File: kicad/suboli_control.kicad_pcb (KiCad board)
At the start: 2 copper layers, 125 x 95 mm, 45 parts, among them J1 DC barrel jack panel header 5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, J2 3.5 mm TRS input panel header, J4 3.5 mm TRS headphone panel he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, J5 MA12070 module power, J6 MA12070 module audio in, SW1 DPST power switch panel header, U1 TLE2426ILP

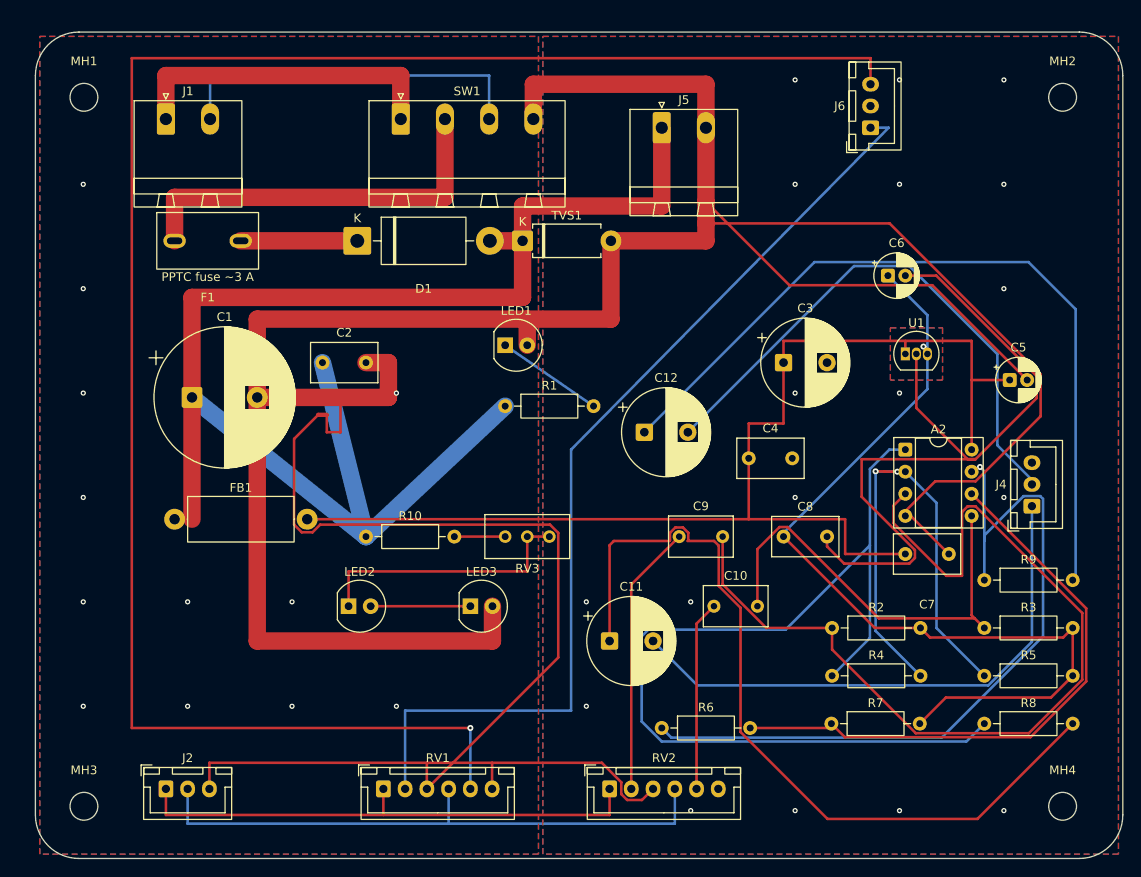
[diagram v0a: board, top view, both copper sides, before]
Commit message: R20: 8mm corner radius + re-export Gerbers + restore BOM
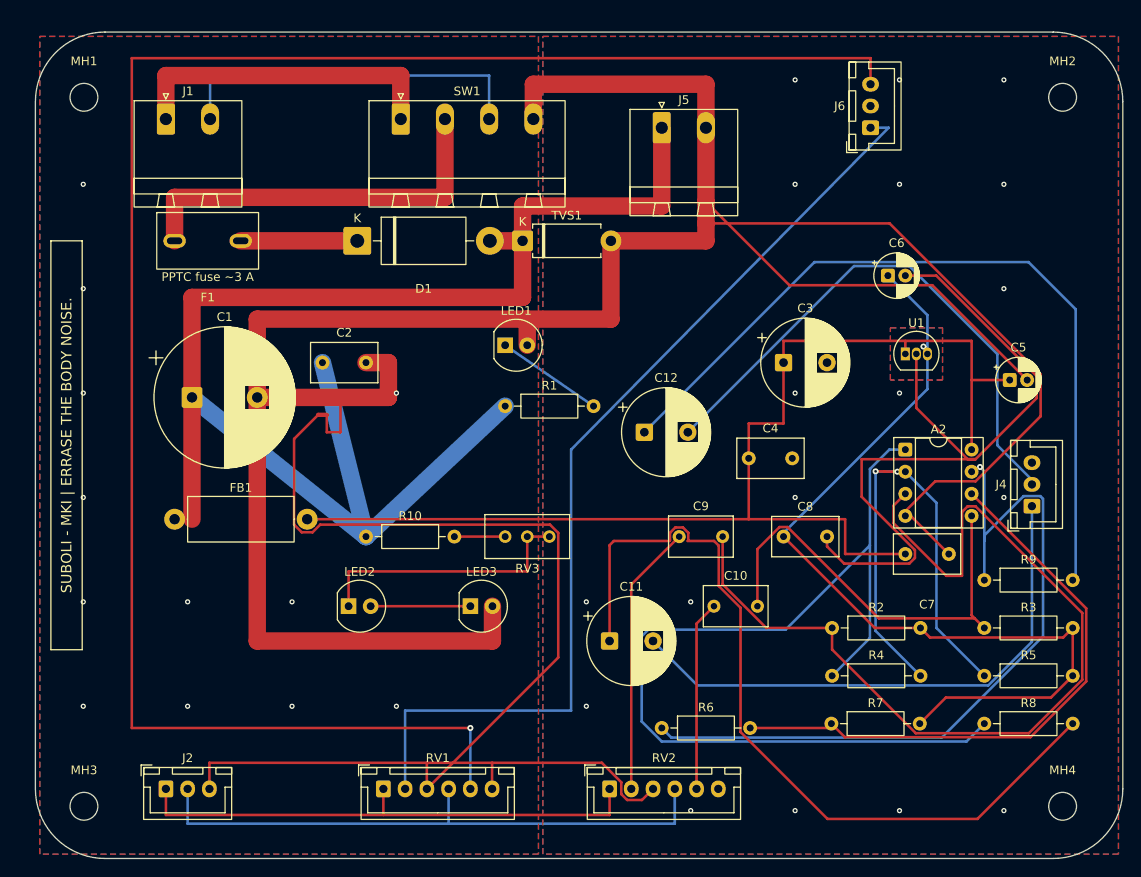
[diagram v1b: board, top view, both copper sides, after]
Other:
- outline, holes or cut-outs redrawn
- board text added: "SUBOLI - MKI | ERRASE THE BODY NOISE."
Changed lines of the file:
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@@
 		)
 	)
+	(gr_line
+		(start 13.7 36)
+		(end 17.3 36)
+		(stroke
+			(width 0.15)
+			(type default)
+		)
+		(layer "F.SilkS")
+	)
+	(gr_line
+		(start 13.7 83)
+		(end 13.7 36)
+		(stroke
+			(width 0.15)
+			(type default)
+		)
+		(layer "F.SilkS")
+	)
+	(gr_line
+		(start 17.3 36)
+		(end 17.3 83)
+		(stroke
+			(width 0.15)
+			(type default)
+		)
+		(layer "F.SilkS")
+	)
+	(gr_line
+		(start 17.3 83)
+		(end 13.7 83)
+		(stroke
+			(width 0.15)
+			(type default)
+		)
+		(layer "F.SilkS")
+	)
 	(gr_arc
-		(start 11.92 17)
-		(mid 13.384466 13.464466)
-		(end 16.92 12)
+		(start 11.92 20)
+		(mid 14.263146 14.343146)
+		(end 19.92 12)
 		(stroke
 			(width 0.15)
@@
 	)
 	(gr_line
-		(start 11.92 102)
-		(end 11.92 17)
+		(start 11.92 99)
+		(end 11.92 20)
 		(stroke
 			(width 0.15)
@@
 	)
 	(gr_line
-		(start 16.92 12)
-		(end 131.92 12)
+		(start 19.92 12)
+		(end 128.92 12)
 		(stroke
 			(width 0.15)
@@
 	)
 	(gr_arc
-		(start 16.92 107)
-		(mid 13.384466 105.535534)
-		(end 11.92 102)
+		(start 19.92 107)
+		(mid 14.263146 104.656854)
+		(end 11.92 99)
 		(stroke
 			(width 0.15)
@@
 	)
 	(gr_arc
-		(start 131.92 12)
-		(mid 135.455534 13.464466)
-		(end 136.92 17)
+		(start 128.92 12)
+		(mid 134.576854 14.343146)
+		(end 136.92 20)
 		(stroke
 			(width 0.15)
@@
 	)
 	(gr_line
-		(start 131.92 107)
-		(end 16.92 107)
+		(start 128.92 107)
+		(end 19.92 107)
 		(stroke
 			(width 0.15)
@@
 	)
 	(gr_line
-		(start 136.92 17)
-		(end 136.92 102)
+		(start 136.92 20)
+		(end 136.92 99)
 		(stroke
 			(width 0.15)
@@
 	)
 	(gr_arc
-		(start 136.92 102)
-		(mid 135.455534 105.535534)
-		(end 131.92 107)
+		(start 136.92 99)
+		(mid 134.576854 104.656854)
+		(end 128.92 107)
 		(stroke
 			(width 0.15)
@@
 		(layer "Edge.Cuts")
 	)
+	(gr_text "SUBOLI - MKI | ERRASE THE BODY NOISE."
+		(at 15.5 59.5 90)
+		(layer "F.SilkS")
+		(effects
+			(font
+				(size 1.2 1.2)
+				(thickness 0.15)
+			)
+		)
+	)
 	(segment

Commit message: R21: rotate J1/SW1/J5 180deg + relocate MH1 + clear connector traces for reroute
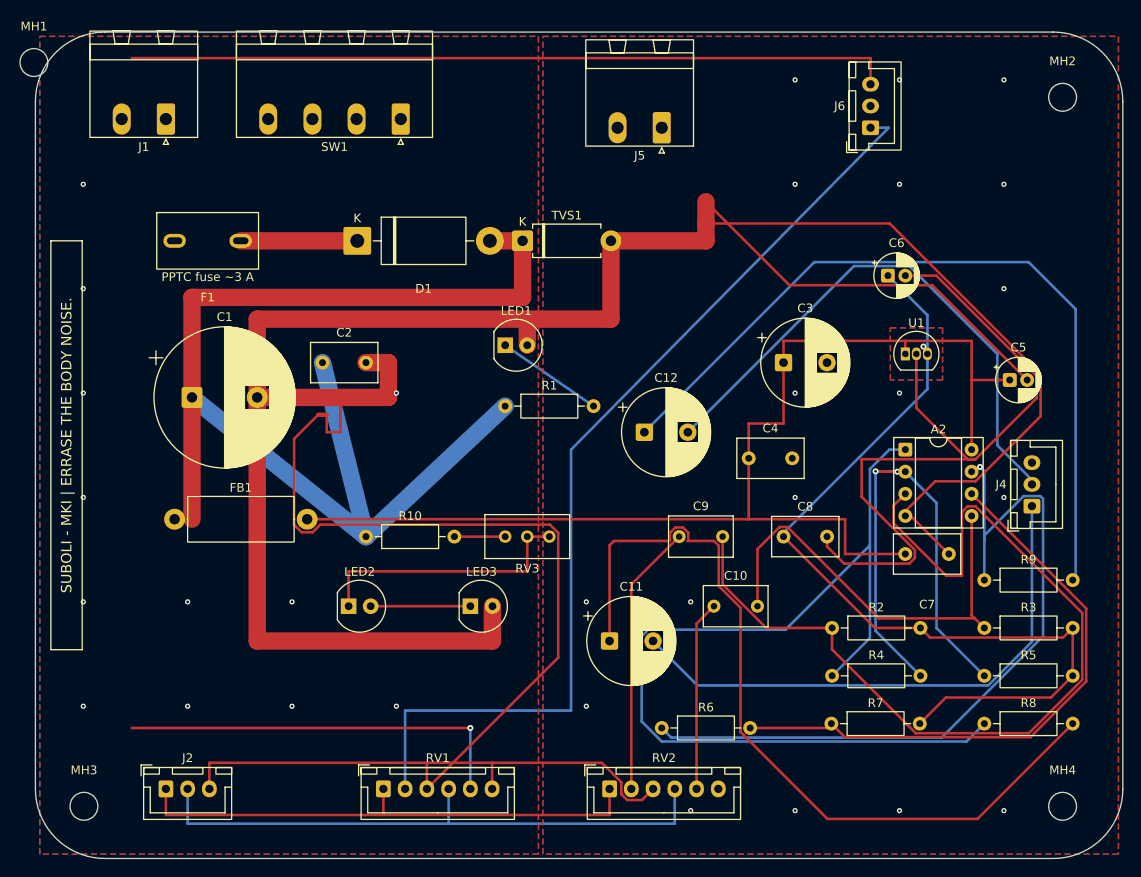
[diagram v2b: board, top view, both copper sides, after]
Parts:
- moved MH1 7.00 mm to (11.8, 15.5)
- turned J1 to 180 degrees
- turned J5 to 180 degrees
- turned SW1 to 180 degrees
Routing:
- net /TACT_INR: track 210.8 -> 133.8 mm
- net /+19V_SW: track 45.1 -> 0.00 mm
- net /GND_RAW: track 42.1 -> 0.00 mm
- net /GND_STAR: track 326.5 -> 289.2 mm
- net /+19V_RAW: track 37.0 -> 0.00 mm
- net /+19V: track 170.9 -> 141.9 mm

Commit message: R22: fix J1/SW1 placement clear of MH1 + reroute
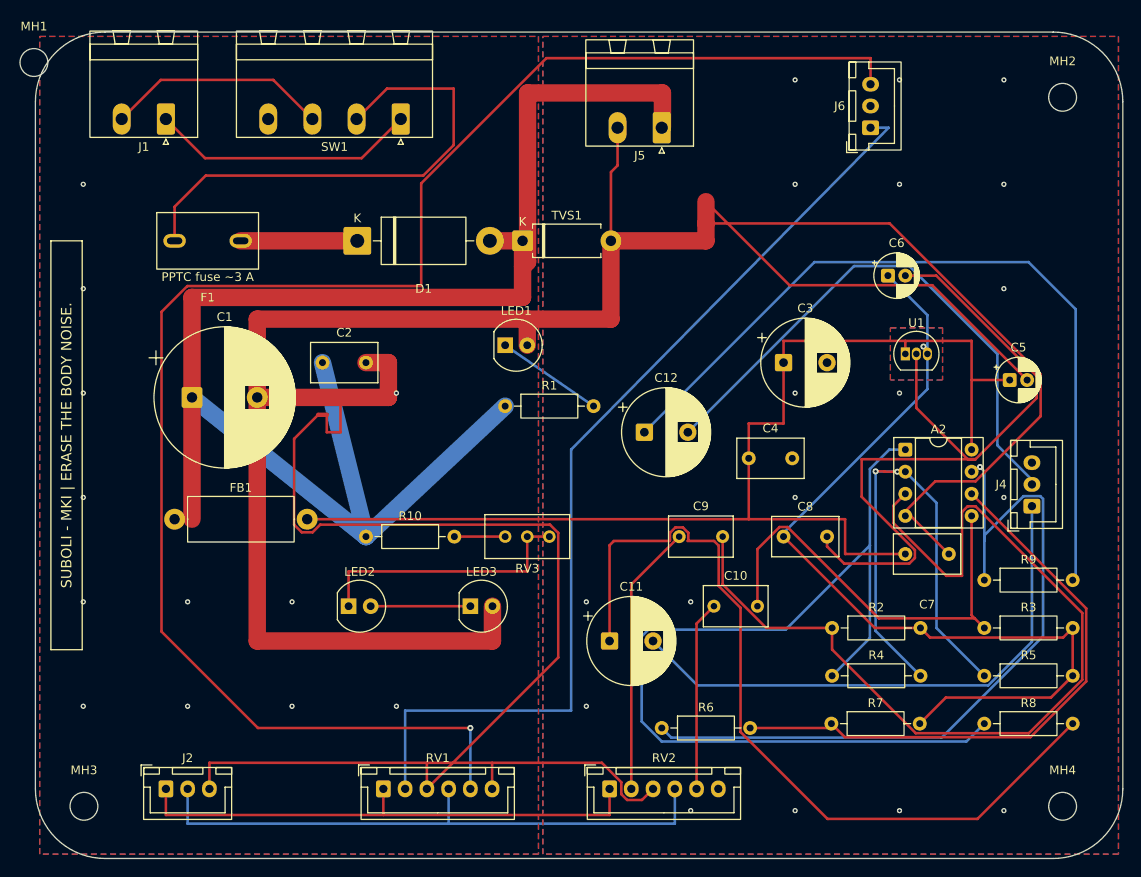
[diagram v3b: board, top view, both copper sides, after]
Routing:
- net /+19V_SW: track 0.00 -> 58.0 mm
- net /TACT_INR: track 133.8 -> 187.3 mm
- net /+19V: track 141.9 -> 181.7 mm
- net /+19V_RAW: track 0.00 -> 30.7 mm
- net /GND_RAW: track 0.00 -> 25.6 mm
- net /GND_STAR: track 289.2 -> 302.5 mm
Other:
- board text added: "SUBOLI - MKI | ERASE THE BODY NOISE."
- board text removed: "SUBOLI - MKI | ERRASE THE BODY NOISE."
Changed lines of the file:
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@@
 		(layer "Edge.Cuts")
 	)
-	(gr_text "SUBOLI - MKI | ERRASE THE BODY NOISE."
+	(gr_text "SUBOLI - MKI | ERASE THE BODY NOISE."
 		(at 15.5 59.5 90)
 		(layer "F.SilkS")
@@
 	)
 	(segment
+		(start 89 36)
+		(end 78.08 36)
+		(width 2)
+		(layer "F.Cu")
+		(net "/GND_STAR")
+	)
+	(segment
 		(start 37.42 54)
 		(end 52.5 54)
@@
 	)
 	(segment
+		(start 78.84 27.34)
+		(end 78.08 28.1)
+		(width 0.3)
+		(layer "F.Cu")
+		(net "/GND_STAR")
+	)
+	(segment
 		(start 52.5 54)
 		(end 52.5 50)
@@
 	)
 	(segment
+		(start 78.84 23)
+		(end 78.84 27.34)
+		(width 0.3)
+		(layer "F.Cu")
+		(net "/GND_STAR")
+	)
+	(segment
 		(start 47 54)
 		(end 47 58)
@@
 	)
 	(segment
+		(start 78.08 28.1)
+		(end 78.08 36)
+		(width 0.3)
+		(layer "F.Cu")
+		(net "/GND_STAR")
+	)
+	(segment
 		(start 47 58)
 		(end 45.42 58)
@@
 	)
 	(segment
-		(start 89 36)
-		(end 89 34)
-		(width 2)
-		(layer "F.Cu")
-		(net "/GND_STAR")
-	)
-	(segment
 		(start 111.62 67.62)
 		(end 111.5 67.5)
@@
 	)
 	(segment
-		(start 78.08 36)
+		(start 89 34)
 		(end 89 36)
 		(width 2)
@@
 	)
 	(segment
+		(start 49.42 26.5)
+		(end 31.42 26.5)
+		(width 0.3)
+		(layer "F.Cu")
+		(net "/+19V_RAW")
+	)
+	(segment
+		(start 31.42 26.5)
+		(end 26.92 22)
+		(width 0.3)
+		(layer "F.Cu")
+		(net "/+19V_RAW")
+	)
+	(segment
+		(start 53.92 22)
+		(end 49.42 26.5)
+		(width 0.3)
+		(layer "F.Cu")
+		(net "/+19V_RAW")
+	)
+	(segment
+		(start 56.5 28.5)
+		(end 31.5 28.5)
+		(width 0.3)
+		(layer "F.Cu")
+		(net "/+19V_SW")
+	)
+	(segment
+		(start 60 18.5)
+		(end 60 25)
+		(width 0.3)
+		(layer "F.Cu")
+		(net "/+19V_SW")
+	)
+	(segment
+		(start 52.34 18.5)
+		(end 60 18.5)
+		(width 0.3)
+		(layer "F.Cu")
+		(net "/+19V_SW")
+	)
+	(segment
+		(start 31.5 28.5)
+		(end 27.92 32.08)
+		(width 0.3)
+		(layer "F.Cu")
+		(net "/+19V_SW")
+	)
+	(segment
+		(start 60 25)
+		(end 56.5 28.5)
+		(width 0.3)
+		(layer "F.Cu")
+		(net "/+19V_SW")
+	)
+	(segment
+		(start 48.84 22)
+		(end 52.34 18.5)
+		(width 0.3)
+		(layer "F.Cu")
+		(net "/+19V_SW")
+	)
+	(segment
+		(start 27.92 32.08)
+		(end 27.92 36)
+		(width 0.3)
+		(layer "F.Cu")
+		(net "/+19V_SW")
+	)
+	(segment
+		(start 26.34 17.5)
+		(end 21.84 22)
+		(width 0.3)
+		(layer "F.Cu")
+		(net "/GND_RAW")
+	)
+	(segment
+		(start 39.26 17.5)
+		(end 26.34 17.5)
+		(width 0.3)
+		(layer "F.Cu")
+		(net "/GND_RAW")
+	)
+	(segment
+		(start 43.76 22)
+		(end 39.26 17.5)
+		(width 0.3)
+		(layer "F.Cu")
+		(net "/GND_RAW")
+	)
+	(segment
 		(start 95.932247 80.5)
 		(end 90.92 75.487753)
@@
 	)
 	(segment
+		(start 67.92 39)
+		(end 67.92 42.5)
+		(width 2)
+		(layer "F.Cu")
+		(net "/+19V")
+	)
+	(segment
 		(start 67.92 36)
-		(end 67.92 42.5)
+		(end 67.92 39)
 		(width 2)
 		(layer "F.Cu")
@@
 	)
 	(segment
+		(start 68.5 19)
+		(end 84 19)
+		(width 2)
+		(layer "F.Cu")
+		(net "/+19V")
+	)
+	(segment
 		(start 67.92 42.5)
 		(end 29.92 42.5)
@@
 	)
 	(segment
+		(start 84 22.92)
+		(end 83.92 23)
+		(width 2)
+		(layer "F.Cu")
+		(net "/+19V")
+	)
+	(segment
+		(start 84 19)
+		(end 84 22.92)
+		(width 2)
+		(layer "F.Cu")
+		(net "/+19V")
+	)
+	(segment
+		(start 67.92 39)
+		(end 68.5 38.42)
+		(width 2)
+		(layer "F.Cu")
+		(net "/+19V")
+	)
+	(segment
+		(start 68.5 38.42)
+		(end 68.5 19)
+		(width 2)
+		(layer "F.Cu")
+		(net "/+19V")
+	)
+	(segment
 		(start 49.92 70)
 		(end 65.92 55)
@@
 	)
 	(segment
+		(start 26.418 80.918)
+		(end 26.418 44.160694)
+		(width 0.3)
+		(layer "F.Cu")
+		(net "/TACT_INR")
+	)
+	(segment
+		(start 37.5 92)
+		(end 26.418 80.918)
+		(width 0.3)
+		(layer "F.Cu")
+		(net "/TACT_INR")
+	)
+	(segment
+		(start 29.380694 41.198)
+		(end 56.272165 41.198)
+		(width 0.3)
+		(layer "F.Cu")
+		(net "/TACT_INR")
+	)
+	(segment
+		(start 56.272165 41.198)
+		(end 56.272165 29.386529)
+		(width 0.3)
+		(layer "F.Cu")
+		(net "/TACT_INR")
+	)
+	(segment
+		(start 56.272165 29.386529)
+		(end 70.658694 15)
+		(width 0.3)
+		(layer "F.Cu")
+		(net "/TACT_INR")
+	)
+	(segment
+		(start 70.658694 15)
+		(end 107.92 15)
+		(width 0.3)
+		(layer "F.Cu")
+		(net "/TACT_INR")
+	)
+	(segment
+		(start 26.418 44.160694)
+		(end 29.380694 41.198)
+		(width 0.3)
+		(layer "F.Cu")
+		(net "/TACT_INR")
+	)
+	(segment
 		(start 61.92 92)
-		(end 23 92)
-		(width 0.3)
-		(layer "F.Cu")
-		(net "/TACT_INR")
-	)
-	(segment
-		(start 23 15)
-		(end 107.92 15)
-		(width 0.3)
-		(layer "F.Cu")
+		(end 37.5 92)
+		(width 0.3)
+		(layer "F.Cu")
